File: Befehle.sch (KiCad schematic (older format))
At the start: 51 parts

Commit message: Schaltplan erweitert
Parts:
- added 4,7k: R, symbol R
- added D? (x6): Led_Small, symbol Led_Small
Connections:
- net labels added: incPC, upPC
- wire segments 60 -> 75
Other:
- moved on the sheet: D?, R?
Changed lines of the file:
@@
 L R R?
 U 1 1 57E93BBB
-P 1850 2050
-F 0 "R?" V 1643 2050 50  0000 C CNN
-F 1 "330" V 1734 2050 50  0000 C CNN
-F 2 "" V 1780 2050 50  0000 C CNN
-F 3 "" H 1850 2050 50  0000 C CNN
-	1    1850 2050
+P 1100 1900
+F 0 "R?" V 893 1900 50  0000 C CNN
+F 1 "330" V 984 1900 50  0000 C CNN
+F 2 "" V 1030 1900 50  0000 C CNN
+F 3 "" H 1100 1900 50  0000 C CNN
+	1    1100 1900
 	0    1    1    0
 $EndComp
@@
 L Led_Small D?
 U 1 1 57E94020
-P 1600 2050
-F 0 "D?" H 1600 1937 50  0000 C CNN
-F 1 "Led_Small" H 1600 1936 50  0001 C CNN
-F 2 "" V 1600 2050 50  0000 C CNN
-F 3 "" V 1600 2050 50  0000 C CNN
-	1    1600 2050
+P 850 1900
+F 0 "D?" H 850 1787 50  0000 C CNN
+F 1 "Led_Small" H 850 1786 50  0001 C CNN
+F 2 "" V 850 1900 50  0000 C CNN
+F 3 "" V 850 1900 50  0000 C CNN
+	1    850  1900
 	-1   0    0    1
 $EndComp
@@
 Wire Wire Line
 	3900 3650 4200 3650
-Wire Wire Line
-	6700 1500 6700 750
-Wire Wire Line
-	6900 1500 6900 750
-Wire Wire Line
-	7100 1500 7100 750
-Wire Wire Line
-	7300 1550 7300 750
 $Comp
 L R R?
@@
 	7550 5850 7550 6000
 Wire Wire Line
-	8750 5550 8750 6050
+	8750 5550 8750 6250
 Connection ~ 5400 5650
 Wire Wire Line
@@
 	0    -1   -1   0
 $EndComp
+Wire Wire Line
+	1400 3550 1400 4250
+Wire Wire Line
+	6700 1500 6550 1500
+Wire Wire Line
+	6550 1500 6550 650
+Wire Wire Line
+	6900 1500 6900 650
+Wire Wire Line
+	7100 1500 7100 1450
+Wire Wire Line
+	7100 1450 7150 1450
+Wire Wire Line
+	7150 1450 7150 650
+Wire Wire Line
+	7300 1500 7400 1500
+Wire Wire Line
+	7400 1500 7400 650
+$Comp
+L Led_Small D?
+U 1 1 580EAA2D
+P 6450 1300
+F 0 "D?" H 6400 1425 50  0000 L CNN
+F 1 "Led_Small" H 6275 1200 50  0000 L CNN
+F 2 "" V 6450 1300 50  0000 C CNN
+F 3 "" V 6450 1300 50  0000 C CNN
+	1    6450 1300
+	1    0    0    -1
+$EndComp
+$Comp
+L Led_Small D?
+U 1 1 580EAB66
+P 6450 1450
+F 0 "D?" H 6400 1575 50  0000 L CNN
+F 1 "Led_Small" H 6275 1350 50  0000 L CNN
+F 2 "" V 6450 1450 50  0000 C CNN
+F 3 "" V 6450 1450 50  0000 C CNN
+	1    6450 1450
+	1    0    0    -1
+$EndComp
+$Comp
+L Led_Small D?
+U 1 1 580EABEB
+P 6800 1450
+F 0 "D?" H 6750 1575 50  0000 L CNN
+F 1 "Led_Small" H 6625 1350 50  0000 L CNN
+F 2 "" V 6800 1450 50  0000 C CNN
+F 3 "" V 6800 1450 50  0000 C CNN
+	1    6800 1450
+	1    0    0    -1
+$EndComp
+$Comp
+L Led_Small D?
+U 1 1 580EAC8E
+P 7050 1300
+F 0 "D?" H 7000 1425 50  0000 L CNN
+F 1 "Led_Small" H 6875 1200 50  0000 L CNN
+F 2 "" V 7050 1300 50  0000 C CNN
+F 3 "" V 7050 1300 50  0000 C CNN
+	1    7050 1300
+	1    0    0    -1
+$EndComp
+$Comp
+L Led_Small D?
+U 1 1 580EAD43
+P 7300 1000
+F 0 "D?" H 7250 1125 50  0000 L CNN
+F 1 "Led_Small" H 7125 900 50  0000 L CNN
+F 2 "" V 7300 1000 50  0000 C CNN
+F 3 "" V 7300 1000 50  0000 C CNN
+	1    7300 1000
+	1    0    0    -1
+$EndComp
+$Comp
+L Led_Small D?
+U 1 1 580EAE00
+P 7300 1200
+F 0 "D?" H 7250 1325 50  0000 L CNN
+F 1 "Led_Small" H 7125 1100 50  0000 L CNN
+F 2 "" V 7300 1200 50  0000 C CNN
+F 3 "" V 7300 1200 50  0000 C CNN
+	1    7300 1200
+	1    0    0    -1
+$EndComp
+Wire Wire Line
+	7200 1000 7200 950
+Connection ~ 7200 950
+Wire Wire Line
+	7200 1200 7200 1100
+Connection ~ 7200 1100
+Wire Wire Line
+	6950 1300 6950 1250
+Connection ~ 6950 1250
+Wire Wire Line
+	6700 1450 6700 1400
+Connection ~ 6700 1400
+Wire Wire Line
+	6350 1450 6350 1400
+Connection ~ 6350 1400
+Wire Wire Line
+	6350 1300 6350 1250
+Connection ~ 6350 1250
+$Comp
+L GND #PWR?
+U 1 1 580EBD54
+P 7250 3200
+F 0 "#PWR?" H 7250 2950 50  0001 C CNN
+F 1 "GND" H 7250 3050 50  0000 C CNN
+F 2 "" H 7250 3200 50  0000 C CNN
+F 3 "" H 7250 3200 50  0000 C CNN
+	1    7250 3200
+	1    0    0    -1
+$EndComp
+$Comp
+L GND #PWR?
+U 1 1 580EC4FA
+P 5600 3350
+F 0 "#PWR?" H 5600 3100 50  0001 C CNN
+F 1 "GND" H 5600 3200 50  0000 C CNN
+F 2 "" H 5600 3350 50  0000 C CNN
+F 3 "" H 5600 3350 50  0000 C CNN
+	1    5600 3350
+	1    0    0    -1
+$EndComp
+$Comp
+L VCC #PWR?
+U 1 1 580EC580
+P 5600 3250
+F 0 "#PWR?" H 5600 3100 50  0001 C CNN
+F 1 "VCC" H 5600 3400 50  0000 C CNN
+F 2 "" H 5600 3250 50  0000 C CNN
+F 3 "" H 5600 3250 50  0000 C CNN
+	1    5600 3250
+	1    0    0    -1
+$EndComp
+Wire Wire Line
+	11150 5650 11150 6100
+Wire Wire Line
+	11150 6100 11050 6100
+Wire Wire Line
+	11050 6100 11050 6200
+Text GLabel 11050 6200 3    60   Input ~ 0
+upPC
+Wire Wire Line
+	8750 6050 9000 6050
+Connection ~ 8750 6050
+Text GLabel 8750 6250 3    60   Input ~ 0
+incPC
+$Comp
+L R 4,7k
+U 1 1 580F54F3
+P 9150 6050
+F 0 "4,7k" V 9230 6050 50  0000 C CNN
+F 1 "R" V 9150 6050 50  0000 C CNN
+F 2 "" V 9080 6050 50  0000 C CNN
+F 3 "" H 9150 6050 50  0000 C CNN
+	1    9150 6050
+	0    -1   1    0
+$EndComp
+$Comp
+L VCC #PWR?
+U 1 1 580F57E4
+P 9300 6050
+F 0 "#PWR?" H 9300 5900 50  0001 C CNN
+F 1 "VCC" H 9300 6200 50  0000 C CNN
+F 2 "" H 9300 6050 50  0000 C CNN
+F 3 "" H 9300 6050 50  0000 C CNN
+	1    9300 6050
+	0    1    1    0
+$EndComp
 $EndSCHEMATC

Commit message: Befehle aktualisiert
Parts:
- added 4,7k? (x2): R, symbol R
- added D? (x2): LED, symbol Led_Small
- added R? (x2): 330, symbol R
- added U? (x2): 74LS04, symbol 74LS04
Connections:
- net labels added: a1, a2, a3, a4, a5, a6, a7, a8, incPCz, loadIR
- wire segments 75 -> 107

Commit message: Befehle Speicherplan fast fertig
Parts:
- added P? (x2): CONN_01X07, Connect:IDC_Header_Straight_20pins, symbol CONN_01X07
- 4,7k, 4,7k? (x2), R? (x21): footprint (none) -> Resistors_ThroughHole:Resistor_Horizontal_RM10mm
- D? (x21): footprint (none) -> LEDs:LED-3MM
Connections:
- net labels added: d1, d2, d3, d4, d5, d6, d7, d8, y1, y2, y3, y4, y5, y6, y7, y8
- wire segments 107 -> 110

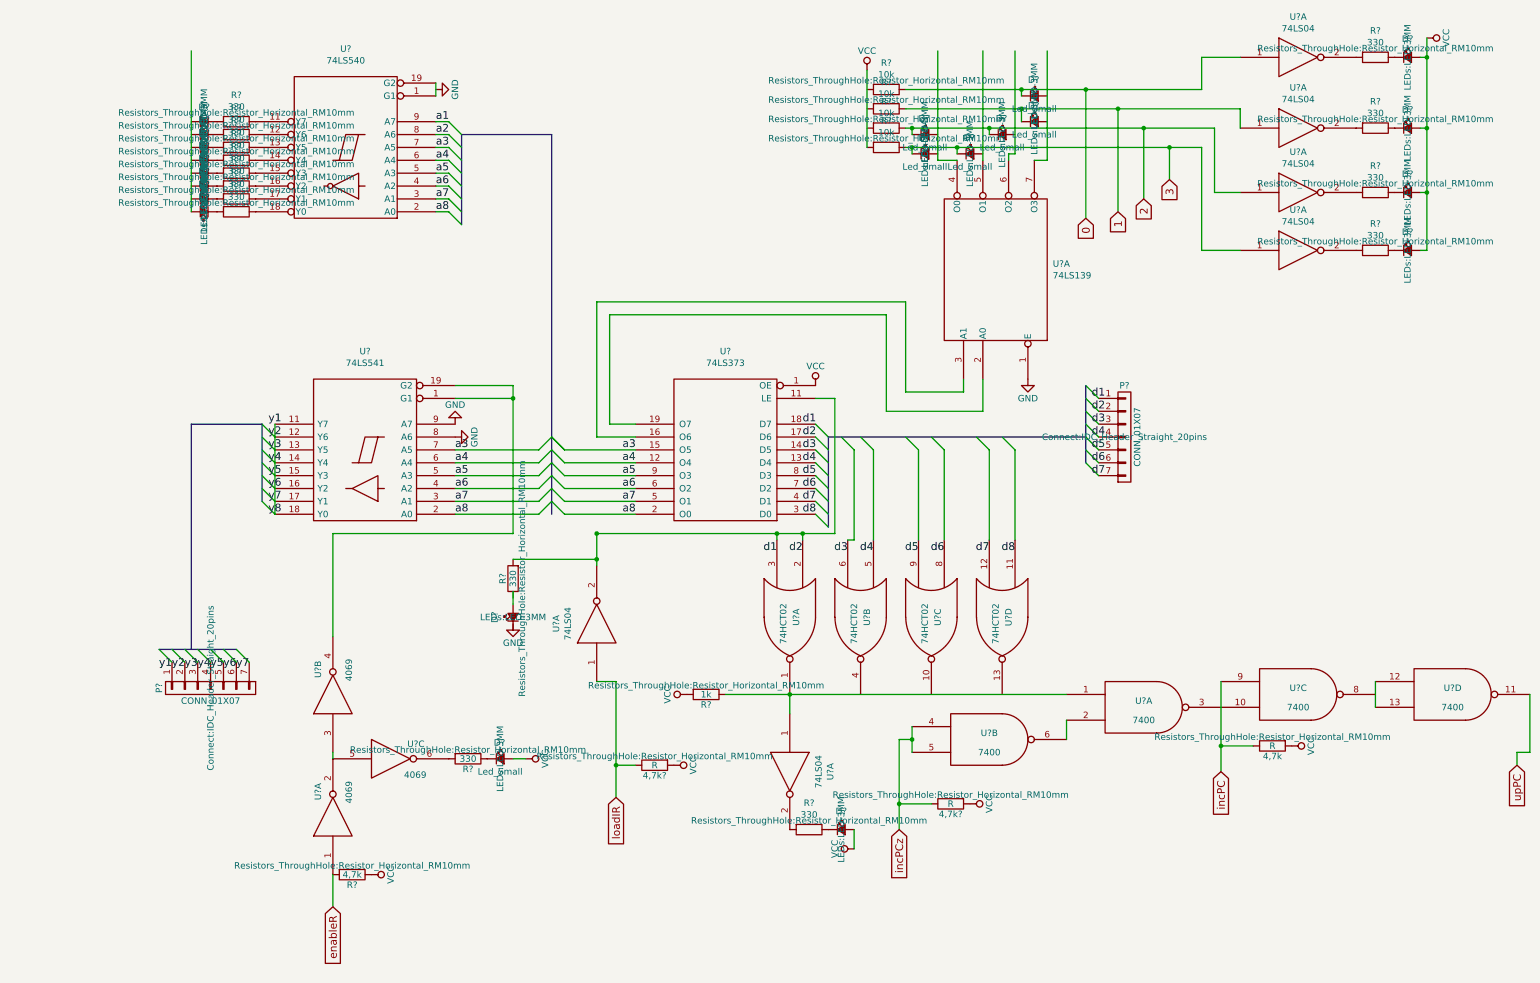
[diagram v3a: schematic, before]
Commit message: Footprints ausgebessert und die Positionierung der Bauteile begonnen
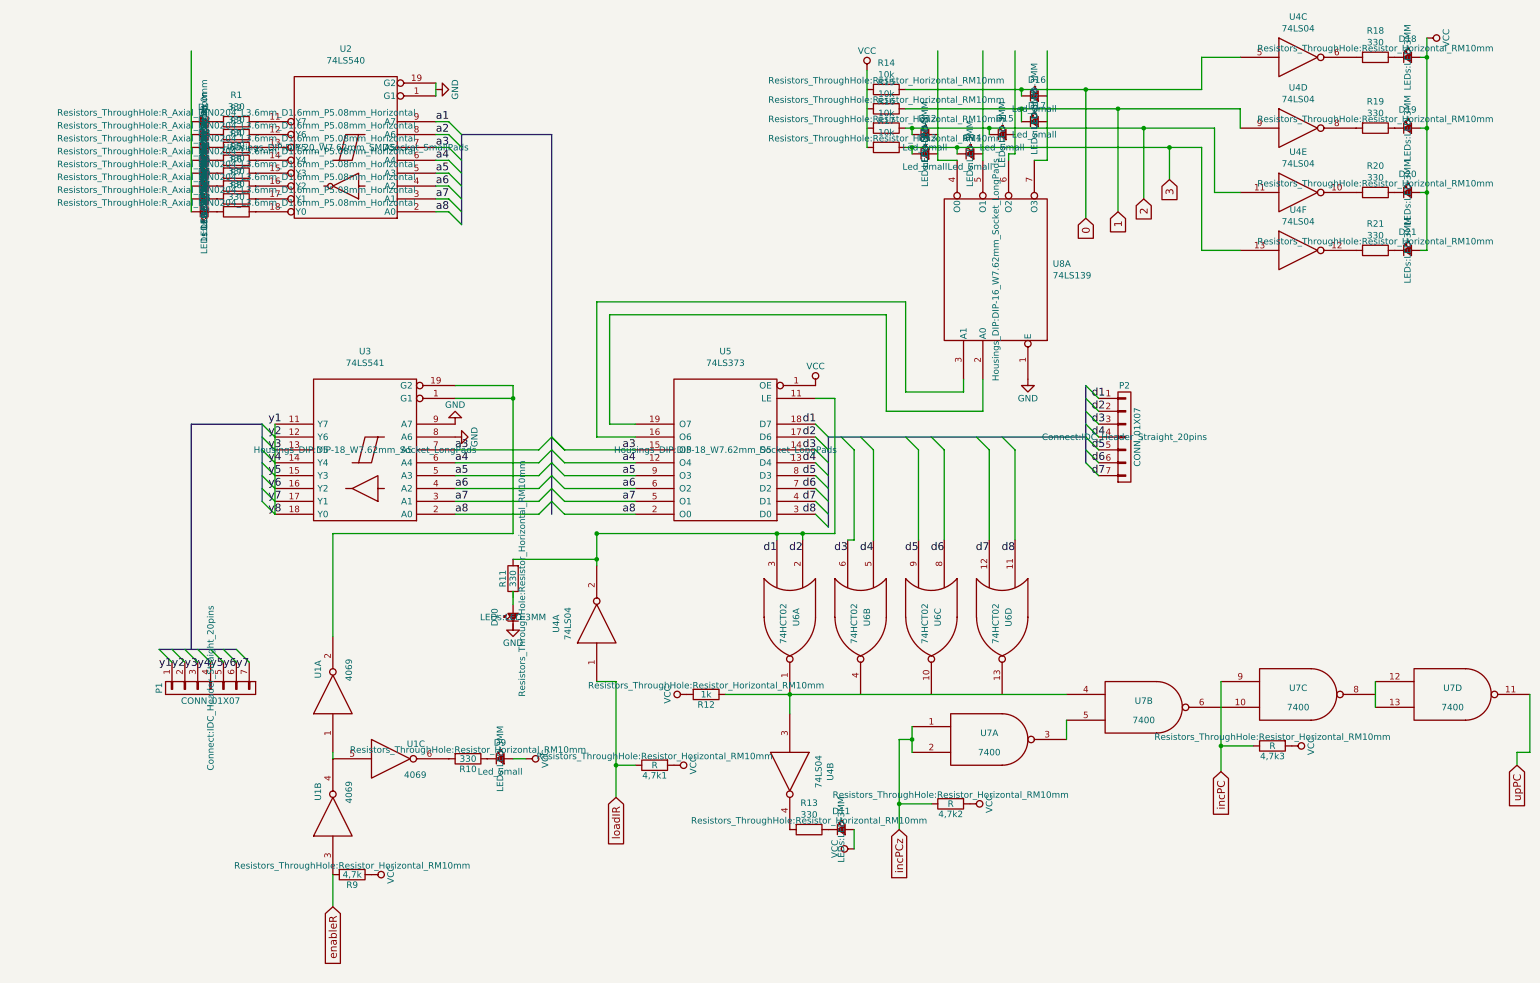
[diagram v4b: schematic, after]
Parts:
- D1, D2, D3, D4, D5, D6, D7, D8: renamed from D?; footprint LEDs:LED-3MM -> LEDs:LED_D3.0mm
- R1, R2, R3, R4, R5, R6, R7, R8: renamed from R?; footprint Resistors_ThroughHole:Resistor_Horizontal_RM10mm -> Resistors_ThroughHole:R_Axial_DIN0204_L3.6mm_D1.6mm_P5.08mm_Horizontal
- U2: renamed from U?; footprint (none) -> Housings_DIP:DIP-20_W7.62mm_SMDSocket_SmallPads
- U3, U5: renamed from U?; footprint (none) -> Housings_DIP:DIP-18_W7.62mm_Socket_LongPads
- U8: renamed from U?; footprint (none) -> Housings_DIP:DIP-16_W7.62mm_Socket_LongPads
- gave numbers to parts that had none: 34
- renumbered 4,7k to 4,7k3

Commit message: Befehle Footprints und Leiterbahnen added
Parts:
- removed P1: CONN_01X07, Connect:IDC_Header_Straight_20pins, symbol CONN_01X07
- added P2: CONN_02X10, symbol CONN_02X10
- renumbered 4,7k2 to 4,7k1, 4,7k1 to 4,7k2, D11 to D1, D4 to D10, D13 to D11, D14 to D12, D3 to D13, D2 to D14, D12 to D15, D15 to D16, D19 to D17, D1 to D18, D17 to D19, D9 to D2, D16 to D20, D18 to D21, D10 to D3, D21 to D4, D8 to D5, D7 to D6, D20 to D7, D6 to D8, D5 to D9, P2 to P1, R9 to R1, R6 to R10, R5 to R11, R4 to R12, R3 to R13, R17 to R14, R2 to R15, R19 to R17, R1 to R18, R15 to R19, R13 to R2, R14 to R20, R18 to R21, R10 to R3, R12 to R4, R11 to R5, R21 to R6, R8 to R7, R7 to R8, R20 to R9, U4 to U2, U7 to U3, U6 to U4, U3 to U5, U5 to U6, U8 to U7, U2 to U8
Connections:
- wire segments 110 -> 141
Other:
- moved on the sheet: 4,7k1, 4,7k2, 4,7k3, D1, D10, D11, D12, D13, D14, D15, D16, D17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

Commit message: bauteile angeordnet
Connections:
- wire segments 141 -> 168
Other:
- moved on the sheet: 4,7k1, 4,7k2, 4,7k3, D1, D10, D11, D12, D13, D14, D15, D16, D17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

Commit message: pcb
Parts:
- removed P1: CONN_01X07, Connect:IDC_Header_Straight_20pins, symbol CONN_01X07
- added P2: CONN_02X10, Connect:IDC_Header_Straight_20pins, symbol CONN_02X10
- P2: footprint (none) -> Connect:IDC_Header_Straight_20pins
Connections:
- net labels added: 11
- wire segments 168 -> 177
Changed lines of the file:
@@
 a8
 Entry Wire Line
-	-6200 4700 -6300 4800
-Entry Wire Line
-	-6300 4700 -6400 4800
-Entry Wire Line
-	-6400 4700 -6500 4800
-Entry Wire Line
-	-6500 4700 -6600 4800
-Entry Wire Line
-	-6600 4700 -6700 4800
-Entry Wire Line
-	-6700 4700 -6800 4800
-Entry Wire Line
-	-6800 4700 -6900 4800
-Entry Wire Line
-	-6900 4700 -7000 4800
+	-6200 4750 -6300 4850
+Entry Wire Line
+	-6300 4750 -6400 4850
+Entry Wire Line
+	-6400 4750 -6500 4850
+Entry Wire Line
+	-6500 4750 -6600 4850
+Entry Wire Line
+	-6600 4750 -6700 4850
+Entry Wire Line
+	-6700 4750 -6800 4850
+Entry Wire Line
+	-6800 4750 -6900 4850
+Entry Wire Line
+	-6900 4750 -7000 4850
 Entry Wire Line
 	-6300 4900 -6400 5000
@@
 Text Label -6800 4600 3    60   ~ 0
 d7
-Text Label -6900 4600 3    60   ~ 0
-d8
 Text Label -7200 4400 1    60   ~ 0
 d1
@@
 Text Label -7200 6250 1    60   ~ 0
 d8
-$Comp
-L CONN_01X07 P1
-U 1 1 5845E2F9
-P -6300 7100
-F 0 "P1" H -6300 7500 50  0000 C CNN
-F 1 "CONN_01X07" V -6200 7100 50  0000 C CNN
-F 2 "Connect:IDC_Header_Straight_20pins" H -6300 7100 50  0000 C CNN
-F 3 "" H -6300 7100 50  0000 C CNN
-	1    -6300 7100
-	0    1    1    0
-$EndComp
 Entry Wire Line
 	-5900 6800 -6000 6900
@@
 F 0 "P2" V -5954 -1338 50  0000 R CNN
 F 1 "CONN_02X10" V -6045 -1338 50  0000 R CNN
-F 2 "" H -6000 -2000 50  0000 C CNN
+F 2 "Connect:IDC_Header_Straight_20pins" H -6000 -2000 50  0000 C CNN
 F 3 "" H -6000 -2000 50  0000 C CNN
 	1    -6000 -800
 	0    -1   -1   0
 $EndComp
+$Comp
+L CONN_02X10 P2
+U 1 1 5A1624C1
+P -6350 7300
+F 0 "P2" V -6304 6762 50  0000 R CNN
+F 1 "CONN_02X10" V -6395 6762 50  0000 R CNN
+F 2 "Connect:IDC_Header_Straight_20pins" H -6350 6100 50  0000 C CNN
+F 3 "" H -6350 6100 50  0000 C CNN
+	1    -6350 7300
+	0    -1   -1   0
+$EndComp
+Text Label -6950 6250 0    60   ~ 0
+11
+Text Label -6900 4750 0    60   ~ 0
+d8
 Wire Wire Line
 	-8100 9350 -8850 9350
@@
 Connection ~ -7650 8250
 Wire Wire Line
-	-7550 8250 -7650 8250
-Wire Wire Line
-	-7650 8250 -7750 8250
+	-7750 8250 -7550 8250
 Wire Wire Line
 	-7650 8150 -7650 8250
@@
 	-9200 -1150 -9050 -1150
 Wire Bus Line
-	-5900 6800 -6000 6800
-Wire Bus Line
-	-6000 6800 -6100 6800
-Wire Bus Line
-	-6100 6800 -6200 6800
-Wire Bus Line
-	-6200 6800 -6300 6800
-Wire Bus Line
-	-6300 6800 -6400 6800
-Wire Bus Line
-	-6400 6800 -6500 6800
+	-6500 6800 -5900 6800
 Connection ~ -7050 4400
 Wire Wire Line
@@
 	-6400 6250 -7100 6250
 Wire Bus Line
-	-6300 4800 -6300 4900
-Wire Bus Line
-	-6300 4900 -6300 5050
-Wire Bus Line
-	-6300 5050 -6300 5400
-Wire Bus Line
-	-6300 5400 -6300 5600
-Wire Bus Line
-	-6300 5600 -6300 5950
-Wire Bus Line
-	-6300 5950 -6300 6150
-Wire Bus Line
-	-6300 6150 -6300 6800
-Wire Bus Line
-	-6300 4800 -6400 4800
-Wire Bus Line
-	-6400 4800 -6500 4800
-Wire Bus Line
-	-6500 4800 -6600 4800
-Wire Bus Line
-	-6600 4800 -6700 4800
-Wire Bus Line
-	-6700 4800 -6800 4800
-Wire Bus Line
-	-6800 4800 -6900 4800
-Wire Bus Line
-	-6900 4800 -7000 4800
-Wire Wire Line
-	-7050 3000 -7250 3000
-Wire Wire Line
-	-7250 3000 -7300 3000
+	-6300 4850 -6300 4950
+Wire Bus Line
+	-6300 4900 -6300 6800
+Wire Bus Line
+	-7000 4850 -6300 4850
+Wire Wire Line
+	-7300 3000 -7050 3000
 Connection ~ -7050 3000
 Wire Wire Line
-	-7050 3000 -7050 4400
-Wire Wire Line
-	-7050 4400 -7050 4600
-Wire Wire Line
-	-7050 4600 -7050 4850
-Wire Wire Line
-	-7050 4850 -6000 4850
+	-7050 3000 -7050 4900
+Wire Wire Line
+	-7050 4900 -6000 4900
 Wire Wire Line
 	-6900 1900 -6900 2550
@@
 	-6900 2750 -6900 3300
 Wire Bus Line
-	-3950 2650 -6300 2650
-Wire Bus Line
-	-6300 2650 -6400 2650
-Wire Bus Line
-	-6400 2650 -6500 2650
-Wire Bus Line
-	-6500 2650 -6600 2650
-Wire Bus Line
-	-6600 2650 -6700 2650
-Wire Bus Line
-	-6700 2650 -6800 2650
-Wire Bus Line
-	-6800 2650 -6900 2650
-Wire Bus Line
-	-3950 1950 -3950 2650
-Wire Bus Line
-	-3950 1950 -4050 1950
-Wire Bus Line
-	-4050 1950 -4150 1950
-Wire Bus Line
-	-4150 1950 -4250 1950
-Wire Bus Line
-	-4250 1950 -4350 1950
-Wire Bus Line
-	-4350 1950 -4450 1950
-Wire Bus Line
-	-4450 1950 -4550 1950
-Wire Bus Line
-	-4550 1950 -4650 1950
+	-6900 2650 -3950 2650
+Wire Bus Line
+	-3950 2650 -3950 1950
+Wire Bus Line
+	-3950 1950 -4650 1950
 Wire Wire Line
 	-3300 -150 -4550 -150
@@
 	-6300 3000 -6300 3300
 Wire Wire Line
-	-3900 5400 -3900 5450
-Wire Wire Line
-	-3900 5450 -3900 6050
-Wire Wire Line
-	-3900 6050 -3900 7250
-Wire Wire Line
-	-3900 7250 -3900 7800
-Wire Wire Line
-	-4050 5400 -4050 5450
-Wire Wire Line
-	-4050 5450 -4050 5800
-Wire Wire Line
-	-4050 5800 -4050 7450
-Wire Wire Line
-	-4050 7450 -4050 7700
-Wire Wire Line
-	-3750 5400 -3750 6300
-Wire Wire Line
-	-3750 6300 -3750 7050
-Wire Wire Line
-	-3750 7050 -3750 8000
-Wire Wire Line
-	-3600 5400 -3600 6300
-Wire Wire Line
-	-3600 6300 -3600 6800
-Wire Wire Line
-	-3600 6800 -3600 7700
+	-3900 5400 -3900 7800
+Wire Wire Line
+	-4050 5400 -4050 7700
+Wire Wire Line
+	-3750 5400 -3750 8000
+Wire Wire Line
+	-3600 5400 -3600 7700
 Wire Wire Line
 	-3600 7700 -3350 7700
@@
 	-4850 9450 -4850 9400
 Wire Wire Line
-	-3200 9450 -3350 9450
-Wire Wire Line
-	-3350 9450 -3900 9450
-Wire Wire Line
-	-3900 9450 -4400 9450
-Wire Wire Line
-	-4400 9450 -4850 9450
+	-4850 9450 -3200 9450
 Wire Wire Line
 	-3350 9450 -3350 9400
@@
 Connection ~ -4400 9450
 Wire Wire Line
-	-8300 4000 -8300 4500
-Wire Wire Line
-	-8300 4500 -8300 6650
+	-8300 4000 -8300 6650
 Wire Wire Line
 	-8500 6650 -8650 6650
 Wire Wire Line
-	-8200 7850 -8700 7850
-Wire Wire Line
-	-8700 7850 -8900 7850
+	-8900 7850 -8200 7850
 Connection ~ -8300 4500
 Wire Wire Line
@@
 	-8800 2350 -8800 2450
 Wire Wire Line
-	-5900 1900 -5900 2350
-Wire Wire Line
-	-5900 2350 -6000 2350
-Wire Wire Line
-	-6000 2350 -7050 2350
+	-5900 2350 -5900 1900
+Wire Wire Line
+	-7050 2350 -5900 2350
 Wire Wire Line
 	-7050 2350 -7050 950
@@
 Connection ~ -8700 7850
 Wire Wire Line
-	-8650 5350 -9150 5350
-Wire Wire Line
-	-9150 5350 -9350 5350
+	-9350 5350 -8650 5350
 Wire Wire Line
 	-9150 5350 -9150 5600
 Connection ~ -9150 5350
 Wire Wire Line
-	-8550 5450 -8650 5450
-Wire Wire Line
-	-8650 5450 -8750 5450
-Wire Wire Line
-	-8650 5450 -8650 5350
+	-8750 5450 -8550 5450
+Wire Wire Line
+	-8650 5350 -8650 5450
 Connection ~ -8650 5450
 Wire Wire Line
 	-9350 5000 -9500 5000
 Wire Wire Line
-	-6000 4850 -6000 4700
-Wire Wire Line
-	-8200 3000 -8200 3150
-Wire Wire Line
-	-8200 3150 -8850 3150
-Wire Wire Line
-	-8850 3150 -9100 3150
+	-6000 4900 -6000 4700
+Wire Wire Line
+	-8200 3150 -8200 3000
+Wire Wire Line
+	-9100 3150 -8200 3150
 Wire Wire Line
 	-8850 3150 -8850 3300
@@
 Wire Wire Line
 	-6350 -550 -6350 -100
+Wire Wire Line
+	-6900 4700 -6900 4750
+Wire Wire Line
+	-6800 4700 -6800 4750
+Wire Wire Line
+	-6700 4700 -6700 4750
+Wire Wire Line
+	-6600 4700 -6600 4750
+Wire Wire Line
+	-6500 4700 -6500 4750
+Wire Wire Line
+	-6400 4700 -6400 4750
+Wire Wire Line
+	-6300 4700 -6300 4750
+Wire Wire Line
+	-6200 4700 -6200 4750
+Wire Wire Line
+	-42900 25500 -42900 40500
+Wire Wire Line
+	-42900 40500 -58500 40500
+Wire Wire Line
+	-58500 40500 -58500 25400
+Wire Wire Line
+	-58500 25400 -42900 25400
+Wire Wire Line
+	-42900 25400 -42900 10550
+Wire Wire Line
+	-42900 10550 -58250 10550
+Wire Wire Line
+	-58250 10550 -58250 20400
+Wire Wire Line
+	-58250 20400 -43000 20400
+Wire Wire Line
+	-43000 20400 -43000 19900
+Wire Wire Line
+	-55050 12950 -55050 15000
+Wire Wire Line
+	-55050 15000 -53000 15000
+Wire Wire Line
+	-53000 15000 -53000 14500
+Wire Wire Line
+	-48750 13500 -48750 15800
+Wire Wire Line
+	-48750 15800 -47000 15800
+Wire Wire Line
+	-53400 18850 -47600 18850
+Wire Wire Line
+	-47600 18850 -47600 17700
+Wire Wire Line
+	-58350 31550 -63100 31550
+Wire Wire Line
+	-63100 31550 -63100 39100
+Wire Wire Line
+	-42250 31650 -36350 31650
+Wire Wire Line
+	-36350 31650 -36350 41900
+Wire Wire Line
+	-47750 40600 -47750 49200
+Wire Wire Line
+	-47750 49200 -49550 49200
+Wire Wire Line
+	-53650 40500 -53650 48450
+Wire Wire Line
+	-53650 48450 -56350 48450
+Connection ~ -53650 40500
 $EndSCHEMATC
